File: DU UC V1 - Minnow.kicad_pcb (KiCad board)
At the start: 2 copper layers, 99 parts, among them J1201 USB_C_Receptacle_USB2.0_16P, J201 SODIMM-260, Q1001 BSS84, Q1201 MMBT3904, Q701 BSS84, Q901 AO3401A, Q902 AO3401A, U1001 MCP2558FD-xSN, U1201 PSM712-LF-T7, U301 3.3, U302 TPS7B8733QKVURQ1, U401 STM32F103CBTx, U501 STM32L552ZET6Q, U701 MCP2558FD-xSN, Y401 8MHz (7pF), Y501 32.768kHz, 1.2pF, Y502 16MHz, 7pF

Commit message: fixed like a bunch of things, power and new xcvr and lights and other goodies, also started layout
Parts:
- removed C1001, C1002, C1103, C1104, C310, C702: 100n, Capacitor_SMD:C_0603_1608Metric_Pad1.08x0.95mm_HandSolder
- removed C307, C308: 22u, Capacitor_SMD:C_0805_2012Metric_Pad1.18x1.45mm_HandSolder
- removed C309: 1u, Capacitor_SMD:C_0402_1005Metric_Pad0.74x0.62mm_HandSolder
- removed D1201: 600m, Diode_SMD:D_SOD-323_HandSoldering
- removed D902: 3V3, Diode_SMD:D_SMB
- removed D903, D904: BZT52C10-TP, Diode_SMD:D_SOD-123
- removed F901, F902: 500mA, Fuse:Fuse_1812_4532Metric
- removed J1201: USB_C_Receptacle_USB2.0_16P, Connector_USB:USB_C_Receptacle_Amphenol_124019772112A
- removed Q1001: BSS84, Package_TO_SOT_SMD:SOT-23
- removed Q1201: MMBT3904, Package_TO_SOT_SMD:SOT-23
- removed Q901, Q902: AO3401A, Package_TO_SOT_SMD:SOT-23-3
- removed R1001: 120, Resistor_SMD:R_0603_1608Metric_Pad0.98x0.95mm_HandSolder
- removed R1201: 10k, Resistor_SMD:R_0402_1005Metric_Pad0.72x0.64mm_HandSolder
- removed R1202: 36k, Resistor_SMD:R_0603_1608Metric_Pad0.98x0.95mm_HandSolder
- removed R1203: 1.5k, Resistor_SMD:R_0402_1005Metric_Pad0.72x0.64mm_HandSolder
- removed R1204, R1205: 5.1k, Resistor_SMD:R_0402_1005Metric_Pad0.72x0.64mm_HandSolder
- removed R1302, R1303, R1304, R1305: 22, Resistor_SMD:R_0402_1005Metric_Pad0.72x0.64mm_HandSolder
- removed U1001: MCP2558FD-xSN, Package_SO:SOIC-8_3.9x4.9mm_P1.27mm
- removed U1201: PSM712-LF-T7, Package_TO_SOT_SMD:SOT-23
- removed U302: TPS7B8733QKVURQ1, Package_TO_SOT_SMD:TO-252-5_TabPin3
- added C1501: 100n, Capacitor_SMD:C_0603_1608Metric_Pad1.08x0.95mm_HandSolder, F.Cu at (259.9, 107.5)
- added C1601: 100n, Capacitor_SMD:C_0402_1005Metric_Pad0.74x0.62mm_HandSolder, F.Cu at (280.4, 126.0)
- added C1602: 100n, Capacitor_SMD:C_0402_1005Metric_Pad0.74x0.62mm_HandSolder, F.Cu at (280.4, 127.9)
- added C1603: 100n, Capacitor_SMD:C_0402_1005Metric_Pad0.74x0.62mm_HandSolder, F.Cu at (280.4, 129.9)
- added C1604: 100n, Capacitor_SMD:C_0402_1005Metric_Pad0.74x0.62mm_HandSolder, F.Cu at (280.4, 131.9)
- added C1605: 100n, Capacitor_SMD:C_0402_1005Metric_Pad0.74x0.62mm_HandSolder, F.Cu at (280.4, 133.8)
- added C503: 100n, Capacitor_SMD:C_0402_1005Metric_Pad0.74x0.62mm_HandSolder, F.Cu at (175.9, 38.1)
- added C526: 4.7u, Capacitor_SMD:C_0603_1608Metric_Pad1.08x0.95mm_HandSolder, F.Cu at (105.7, 84.3)
- added C901: 100n, Capacitor_SMD:C_0402_1005Metric_Pad0.74x0.62mm_HandSolder, F.Cu at (136.4, 130.0)
- added C902: 100n, Capacitor_SMD:C_0402_1005Metric_Pad0.74x0.62mm_HandSolder, F.Cu at (138.6, 130.0)
- added C903: 100n, Capacitor_SMD:C_0402_1005Metric_Pad0.74x0.62mm_HandSolder, F.Cu at (137.5, 130.0)
- added D1101: Red, Diode_SMD:D_0603_1608Metric_Pad1.05x0.95mm_HandSolder, F.Cu at (157.8, 165.9)
- added D1102: Red, Diode_SMD:D_0603_1608Metric_Pad1.05x0.95mm_HandSolder, F.Cu at (154.1, 165.9)
- added D1103: Red, Diode_SMD:D_0603_1608Metric_Pad1.05x0.95mm_HandSolder, F.Cu at (156.0, 165.9)
- added D1104: Red, Diode_SMD:D_0603_1608Metric_Pad1.05x0.95mm_HandSolder, F.Cu at (159.7, 165.9)
- added D1105: Red, Diode_SMD:D_0603_1608Metric_Pad1.05x0.95mm_HandSolder, F.Cu at (152.2, 165.9)
- added D1106: Red, Diode_SMD:D_0603_1608Metric_Pad1.05x0.95mm_HandSolder, F.Cu at (146.6, 165.9)
- added D1107: Red, Diode_SMD:D_0603_1608Metric_Pad1.05x0.95mm_HandSolder, F.Cu at (150.4, 165.9)
- added D1108: Red, Diode_SMD:D_0603_1608Metric_Pad1.05x0.95mm_HandSolder, F.Cu at (148.5, 165.9)
- added D1301: Green, Diode_SMD:D_0805_2012Metric_Pad1.15x1.40mm_HandSolder, F.Cu at (249.1, 54.8)
- added D1401: 20V, Diode_SMD:D_SMB, F.Cu at (342.9, 82.8)
- added D1402: 20V, Diode_SMD:D_SMB, F.Cu at (316.1, 122.0)
- added D1501: White, Diode_SMD:D_0603_1608Metric_Pad1.05x0.95mm_HandSolder, F.Cu at (255.9, 98.8)
- added D1502: White, Diode_SMD:D_0603_1608Metric_Pad1.05x0.95mm_HandSolder, F.Cu at (255.9, 101.4)
- added D1701: 600m, Diode_SMD:D_SOD-323_HandSoldering, F.Cu at (327.5, 134.3)
- added D701: White, Diode_SMD:D_0603_1608Metric_Pad1.05x0.95mm_HandSolder, F.Cu at (232.6, 128.4)
- added D702: White, Diode_SMD:D_0603_1608Metric_Pad1.05x0.95mm_HandSolder, F.Cu at (243.4, 128.3)
- added J1701: MicroUSB, Connector_USB:USB_Micro-B_Amphenol_10118194-0001LF_Horizontal, F.Cu at (325.0, 151.4)
- added J1801: Conn_01x06_Pin, Connector_PinHeader_2.54mm:PinHeader_1x06_P2.54mm_Vertical, F.Cu at (313.6, 46.7)
- added J1802: Conn_01x04_Pin, Connector_PinHeader_2.54mm:PinHeader_1x04_P2.54mm_Vertical, F.Cu at (318.2, 46.7)
- added JP1001: NORFLASH_CLK, Jumper:SolderJumper-3_P1.3mm_Bridged2Bar12_Pad1.0x1.5mm_NumberLabels, F.Cu at (58.4, 92.5)
- added JP1002: NORFLASH_MISO, Jumper:SolderJumper-3_P1.3mm_Bridged2Bar12_Pad1.0x1.5mm_NumberLabels, F.Cu at (58.4, 96.0)
- added JP1003: NORFLASH_MOSI, Jumper:SolderJumper-3_P1.3mm_Bridged2Bar12_Pad1.0x1.5mm_NumberLabels, F.Cu at (58.4, 99.6)
- added JP1004: NORFLASH_NSS, Jumper:SolderJumper-3_P1.3mm_Bridged2Bar12_Pad1.0x1.5mm_NumberLabels, F.Cu at (58.4, 103.2)
- added JP1201: LEDARR_EN, Jumper:SolderJumper-3_P1.3mm_Bridged2Bar12_Pad1.0x1.5mm_NumberLabels, B.Cu at (125.8, 90.6)
- added JP1202: LEDARR_A0, Jumper:SolderJumper-3_P1.3mm_Bridged2Bar12_Pad1.0x1.5mm_NumberLabels, B.Cu at (125.8, 87.0)
- added JP1203: LEDARR_A1, Jumper:SolderJumper-3_P1.3mm_Bridged2Bar12_Pad1.0x1.5mm_NumberLabels, B.Cu at (125.8, 83.5)
- added JP1204: LEDARR_A2, Jumper:SolderJumper-3_P1.3mm_Bridged2Bar12_Pad1.0x1.5mm_NumberLabels, B.Cu at (125.8, 79.9)
- added JP1501: CAN_TERM, Jumper:SolderJumper-2_P1.3mm_Open_RoundedPad1.0x1.5mm, F.Cu at (251.0, 108.5)
- added JP1801: SolderJumper_2_Bridged, Jumper:SolderJumper-2_P1.3mm_Bridged_Pad1.0x1.5mm, F.Cu at (304.8, 46.2)
- added JP1802: SolderJumper_2_Bridged, Jumper:SolderJumper-2_P1.3mm_Bridged_Pad1.0x1.5mm, F.Cu at (304.8, 49.8)
- added JP1803: SolderJumper_2_Bridged, Jumper:SolderJumper-2_P1.3mm_Bridged_Pad1.0x1.5mm, F.Cu at (304.8, 53.3)
- added JP1804: SolderJumper_2_Bridged, Jumper:SolderJumper-2_P1.3mm_Bridged_Pad1.0x1.5mm, F.Cu at (304.8, 56.9)
- added JP1805: SolderJumper_2_Open, Jumper:SolderJumper-2_P1.3mm_Open_Pad1.0x1.5mm, F.Cu at (304.8, 60.4)
- added JP1806: SolderJumper_2_Open, Jumper:SolderJumper-2_P1.3mm_Open_Pad1.0x1.5mm, F.Cu at (309.1, 46.2)
- added JP1807: SolderJumper_2_Open, Jumper:SolderJumper-2_P1.3mm_Open_Pad1.0x1.5mm, F.Cu at (309.1, 49.8)
- added JP1808: SolderJumper_2_Open, Jumper:SolderJumper-2_P1.3mm_Open_Pad1.0x1.5mm, F.Cu at (309.1, 53.3)
- added JP301: AVDD_SEL, Jumper:SolderJumper-3_P1.3mm_Bridged2Bar12_Pad1.0x1.5mm_NumberLabels, F.Cu at (243.2, 44.5)
- added JP501: VDDUSB_SEL, Jumper:SolderJumper-3_P1.3mm_Bridged2Bar12_Pad1.0x1.5mm_NumberLabels, B.Cu at (72.5, 126.3)
- added JP502: VREF_SEL, Jumper:SolderJumper-3_P1.3mm_Bridged2Bar12_Pad1.0x1.5mm_NumberLabels, B.Cu at (72.5, 129.9)
- added JP503: VDDIO_SEL, Jumper:SolderJumper-3_P1.3mm_Bridged2Bar12_Pad1.0x1.5mm_NumberLabels, B.Cu at (72.5, 133.4)
- added JP504: JT_RST_SEL, Jumper:SolderJumper-3_P1.3mm_Bridged2Bar12_Pad1.0x1.5mm_NumberLabels, B.Cu at (72.5, 137.0)
- added JP701: CAN_TERM, Jumper:SolderJumper-2_P1.3mm_Open_RoundedPad1.0x1.5mm, F.Cu at (237.2, 126.4)
- added L501: 4.7u, bfr_inductors:BWVS005050404R7M00, F.Cu at (106.8, 88.3)
- added NT101: NetTie_2, NetTie:NetTie-2_SMD_Pad2.0mm, F.Cu at (173.0, 86.0)
- added Q1301: BSS84, Package_TO_SOT_SMD:SOT-23, F.Cu at (251.6, 55.0)
- added Q1501: BSS84, Package_TO_SOT_SMD:SOT-23, F.Cu at (251.2, 99.9)
- added Q1502: BSS84, Package_TO_SOT_SMD:SOT-23, F.Cu at (251.2, 104.5)
- added Q1701: MMBT3904, Package_TO_SOT_SMD:SOT-23, F.Cu at (322.5, 135.2)
- added Q702: BSS84, Package_TO_SOT_SMD:SOT-23, F.Cu at (241.6, 132.5)
- added R1101: 220, Resistor_SMD:R_0402_1005Metric_Pad0.72x0.64mm_HandSolder, F.Cu at (157.8, 162.8)
- added R1102: 220, Resistor_SMD:R_0402_1005Metric_Pad0.72x0.64mm_HandSolder, F.Cu at (154.1, 162.8)
- added R1103: 220, Resistor_SMD:R_0402_1005Metric_Pad0.72x0.64mm_HandSolder, F.Cu at (156.0, 162.8)
- added R1104: 220, Resistor_SMD:R_0402_1005Metric_Pad0.72x0.64mm_HandSolder, F.Cu at (159.7, 162.8)
- added R1105: 220, Resistor_SMD:R_0402_1005Metric_Pad0.72x0.64mm_HandSolder, F.Cu at (152.2, 162.8)
- added R1106: 220, Resistor_SMD:R_0402_1005Metric_Pad0.72x0.64mm_HandSolder, F.Cu at (146.6, 162.8)
- added R1107: 220, Resistor_SMD:R_0402_1005Metric_Pad0.72x0.64mm_HandSolder, F.Cu at (150.4, 162.8)
- added R1108: 220, Resistor_SMD:R_0402_1005Metric_Pad0.72x0.64mm_HandSolder, F.Cu at (148.5, 162.8)
- added R1401: 470, Resistor_SMD:R_0402_1005Metric_Pad0.72x0.64mm_HandSolder, F.Cu at (312.4, 119.1)
- added R1402: 360, Resistor_SMD:R_0603_1608Metric_Pad0.98x0.95mm_HandSolder, F.Cu at (312.4, 117.5)
- added R1403: 390, Resistor_SMD:R_0603_1608Metric_Pad0.98x0.95mm_HandSolder, F.Cu at (318.4, 116.7)
- added R1404: 270, Resistor_SMD:R_0603_1608Metric_Pad0.98x0.95mm_HandSolder, F.Cu at (347.4, 81.1)
- added R1405: 360, Resistor_SMD:R_0603_1608Metric_Pad0.98x0.95mm_HandSolder, F.Cu at (347.4, 83.6)
- added R1406: 390, Resistor_SMD:R_0603_1608Metric_Pad0.98x0.95mm_HandSolder, F.Cu at (347.4, 86.2)
- added R1407: 100k, Resistor_SMD:R_0402_1005Metric_Pad0.72x0.64mm_HandSolder, F.Cu at (316.1, 116.4)
- added R1408: 100k, Resistor_SMD:R_0402_1005Metric_Pad0.72x0.64mm_HandSolder, F.Cu at (351.2, 82.9)
- added R1501: 120, Resistor_SMD:R_0402_1005Metric_Pad0.72x0.64mm_HandSolder, F.Cu at (260.5, 103.7)
- added R1502: 120, Resistor_SMD:R_0603_1608Metric_Pad0.98x0.95mm_HandSolder, F.Cu at (260.3, 98.8)
- added R1503: 120, Resistor_SMD:R_0603_1608Metric_Pad0.98x0.95mm_HandSolder, F.Cu at (260.3, 101.3)
- added R1701: 10k, Resistor_SMD:R_0402_1005Metric_Pad0.72x0.64mm_HandSolder, F.Cu at (317.4, 147.3)
- added R1702: 36k, Resistor_SMD:R_0603_1608Metric_Pad0.98x0.95mm_HandSolder, F.Cu at (318.5, 144.8)
- added R1703: 1.5k, Resistor_SMD:R_0402_1005Metric_Pad0.72x0.64mm_HandSolder, F.Cu at (317.4, 139.7)
- added R1704: 100k, Resistor_SMD:R_0402_1005Metric_Pad0.72x0.64mm_HandSolder, F.Cu at (317.4, 137.1)
- added R1801: 10k, Resistor_SMD:R_0402_1005Metric_Pad0.72x0.64mm_HandSolder, F.Cu at (322.1, 45.4)
- added R1802: 22, Resistor_SMD:R_0402_1005Metric_Pad0.72x0.64mm_HandSolder, F.Cu at (322.1, 47.4)
- added R1803: 22, Resistor_SMD:R_0402_1005Metric_Pad0.72x0.64mm_HandSolder, F.Cu at (322.1, 49.4)
- added R1804: 22, Resistor_SMD:R_0402_1005Metric_Pad0.72x0.64mm_HandSolder, F.Cu at (322.1, 51.4)
- added R1805: 22, Resistor_SMD:R_0402_1005Metric_Pad0.72x0.64mm_HandSolder, F.Cu at (322.1, 53.4)
- added R702: 120, Resistor_SMD:R_0603_1608Metric_Pad0.98x0.95mm_HandSolder, F.Cu at (234.5, 128.4)
- added R703: 120, Resistor_SMD:R_0603_1608Metric_Pad0.98x0.95mm_HandSolder, F.Cu at (241.6, 128.3)
- added R903: 47k, Resistor_SMD:R_0402_1005Metric_Pad0.72x0.64mm_HandSolder, F.Cu at (137.5, 138.0)
- added R904: 47k, Resistor_SMD:R_0402_1005Metric_Pad0.72x0.64mm_HandSolder, F.Cu at (129.0, 133.1)
- added R905: 47k, Resistor_SMD:R_0402_1005Metric_Pad0.72x0.64mm_HandSolder, F.Cu at (129.0, 135.6)
- added R906: 47k, Resistor_SMD:R_0402_1005Metric_Pad0.72x0.64mm_HandSolder, F.Cu at (139.9, 133.1)
- added SW401: STLINK_RST, Button_Switch_SMD:SW_Push_1P1T-SH_NO_CK_KMR2xxG, F.Cu at (260.9, 147.7)
- added SW501: MCU_RST, Button_Switch_SMD:SW_Push_1P1T-SH_NO_CK_KMR2xxG, F.Cu at (72.0, 142.3)
- added U1101: 74HC4051, Package_SO:TSSOP-16_4.4x5mm_P0.65mm, F.Cu at (153.2, 157.6)
- added U1401: TPS25961, Package_SON:WSON-6-1EP_2x2mm_P0.65mm_EP1x1.6mm, F.Cu at (316.1, 118.4)
- added U1402: TPS25961, Package_SON:WSON-6-1EP_2x2mm_P0.65mm_EP1x1.6mm, F.Cu at (351.7, 85.7)
- added U1501: TCAN334G, Package_TO_SOT_SMD:TSOT-23-8, F.Cu at (256.3, 105.1)
- added U1701: PSM712-LF-T7, Package_TO_SOT_SMD:SOT-23, F.Cu at (322.5, 139.9)
- added U901: MX25R3235FM2xx1, Package_SO:SOIC-8_5.3x5.3mm_P1.27mm, F.Cu at (134.5, 134.3)
- C1101, C1102, C520: footprint Capacitor_SMD:C_0603_1608Metric_Pad1.08x0.95mm_HandSolder -> Capacitor_SMD:C_0402_1005Metric_Pad0.74x0.62mm_HandSolder
- C203, C204, R401, R402, R407, R408: moved to B.Cu
- C301, C303: value 22u -> 1u; footprint Capacitor_SMD:C_0805_2012Metric_Pad1.18x1.45mm_HandSolder -> Capacitor_SMD:C_0402_1005Metric_Pad0.74x0.62mm_HandSolder
- C304, C305, C306: value 100n -> 1u; footprint Capacitor_SMD:C_0603_1608Metric_Pad1.08x0.95mm_HandSolder -> Capacitor_SMD:C_0402_1005Metric_Pad0.74x0.62mm_HandSolder
- C509: value 100n -> 22p
- C511: value 22p -> 100n
- C512, C514, C515, C516, C519, C522: value 1u -> 100n
- C517: value 1u -> 100n; footprint Capacitor_SMD:C_0402_1005Metric_Pad0.74x0.62mm_HandSolder -> Capacitor_SMD:C_0603_1608Metric_Pad1.08x0.95mm_HandSolder
- C518, C521, C523, C524: value 10u -> 100n; footprint Capacitor_SMD:C_0603_1608Metric_Pad1.08x0.95mm_HandSolder -> Capacitor_SMD:C_0402_1005Metric_Pad0.74x0.62mm_HandSolder
- C525: value 4.7u -> 100n; footprint Capacitor_SMD:C_0603_1608Metric_Pad1.08x0.95mm_HandSolder -> Capacitor_SMD:C_0402_1005Metric_Pad0.74x0.62mm_HandSolder
- D901: value 4V7 -> 3V3; footprint Diode_SMD:D_SMB -> Diode_SMD:D_SOD-123
- J201: footprint Connector_PCBEdge:SODIMM-260_DDR4_H4.0-5.2_OrientationStd_Socket -> bfr_connectors:SODIMM-260 DDR4
- R1301: value 10k -> 120; footprint Resistor_SMD:R_0402_1005Metric_Pad0.72x0.64mm_HandSolder -> Resistor_SMD:R_0603_1608Metric_Pad0.98x0.95mm_HandSolder
- R701: footprint Resistor_SMD:R_0603_1608Metric_Pad0.98x0.95mm_HandSolder -> Resistor_SMD:R_0402_1005Metric_Pad0.72x0.64mm_HandSolder
- R901, R902: value 100k -> 47k; footprint Resistor_SMD:R_0603_1608Metric_Pad0.98x0.95mm_HandSolder -> Resistor_SMD:R_0402_1005Metric_Pad0.72x0.64mm_HandSolder
- U301: value 3.3 -> TPS7B8733QKVURQ1; footprint Package_TO_SOT_SMD:SOT-223-3_TabPin2 -> Package_TO_SOT_SMD:TO-252-5_TabPin3
- U701: value MCP2558FD-xSN -> TCAN334G; footprint Package_SO:SOIC-8_3.9x4.9mm_P1.27mm -> Package_TO_SOT_SMD:TSOT-23-8
- Y401: value 8MHz (7pF) -> 8MHz 5pF; footprint Crystal:Crystal_HC49-4H_Vertical -> Crystal:Crystal_SMD_5032-2Pin_5.0x3.2mm_HandSoldering
- moved C517 153.6 mm to (66.5, 134.5)
- moved U401 132.0 mm to (269.1, 139.8)
- moved C514 131.3 mm to (85.8, 52.5)
- moved C519 130.7 mm to (89.1, 50.5)
- moved C522 129.5 mm to (89.1, 56.4)
- moved R501 124.1 mm to (94.7, 118.8)
- moved C504 117.7 mm to (98.0, 46.3)
- moved C506 117.7 mm to (98.0, 50.2)
- moved C512 116.2 mm to (101.3, 50.2)
- moved C203 114.0 mm to (82.0, 72.4), turned to -90 degrees
- moved C202 113.9 mm to (82.0, 72.4), turned to 90 degrees
- moved Y501 113.3 mm to (107.9, 124.6)
- moved C204 112.6 mm to (83.6, 72.4), turned to -90 degrees
- moved C201 112.3 mm to (83.6, 72.4), turned to 90 degrees
- moved C1101 106.2 mm to (155.5, 153.0)
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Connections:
- net /Power/3V3_RAW renamed /5V_RAW
- net /Power/5V_RAW renamed /3V3A_RAW
- C1101 pad 1: +3.3V -> GND
- C1101 pad 2: GND -> +3.3V
- C1102 pad 1: +3.3V -> GND
- C1102 pad 2: GND -> +3.3V
- C201 pad 1: GNDPWR -> GND
- C202 pad 1: GNDPWR -> GND
- C301 pad 1: +5V -> /Power/Power Protection/5V_PROT
- C302 pad 1: +5V -> /Power/Power Protection/5V_PROT
- C303 pad 1: Net-(JP301-B) -> /Power/Power Protection/5V_PROT
- C304 pad 1: +5V -> +3.3V
- C305 pad 1: Net-(JP301-B) -> +3.3V
- C504 pad 1: +3.3VA -> +3.3V
- C505 pad 1: +3.3V -> +3.3VA
- C506 pad 1: +3.3VA -> +3.3V
- C507 pad 1: +3.3V -> +3.3VA
- C508 pad 1: +3.3VA -> +3.3V
- C509 pad 1: +3.3V -> Net-(U501I-PH0/HSE_OSC_IN)
- C510 pad 1: Net-(U501I-PH0/HSE_OSC_IN) -> Net-(U501I-PH1/HSE_OSC_OUT)
- C511 pad 1: Net-(U501I-PH1/HSE_OSC_OUT) -> +3.3VA
- C512 pad 1: +3.3VA -> +3.3V
- C513 pad 1: +3.3V -> +3.3VA
- C514 pad 1: +3.3VA -> +3.3V
- C515 pad 1: +3.3V -> +3.3VA
- C516 pad 1: +3.3VA -> +3.3V
- C517 pad 1: +3.3V -> Net-(JP504-A)
- C520 pad 1: Net-(JP504-A) -> +3.3VA
- C521 pad 1: +3.3VA -> +3.3V
- C525 pad 1: Net-(C525-Pad1) -> +3.3V
- C701 pad 1: /STM32L552ZET6Q/Peripherals/+5V -> +3.3V
- D901 pad 1: Net-(D901-K) -> +3.3V
- D901 pad 2: GNDPWR -> GND
- J201 pad 102: /SODIMM Connector/PB15 -> /SODIMM Connector/PB2
- J201 pad 103: /SODIMM Connector/PB0 -> /SODIMM Connector/PC9
- J201 pad 106: /SODIMM Connector/PD1 -> /SODIMM Connector/PB1
- J201 pad 107: /SODIMM Connector/PC0 -> /SODIMM Connector/PC10
- J201 pad 11: GNDPWR -> GND
- J201 pad 110: /SODIMM Connector/PD2 -> /SODIMM Connector/PB0
- J201 pad 111: /SODIMM Connector/PC1 -> /SODIMM Connector/PC11
- J201 pad 114: /SODIMM Connector/PD3 -> /SODIMM Connector/PA7
- J201 pad 115: /SODIMM Connector/PC2 -> /SODIMM Connector/PC12
- J201 pad 118: /SODIMM Connector/PD4 -> /SODIMM Connector/PA6
- J201 pad 119: /SODIMM Connector/PC3 -> /SODIMM Connector/PA8
- J201 pad 122: /SODIMM Connector/PD5 -> /SODIMM Connector/PA5
- J201 pad 123: /SODIMM Connector/PC6 -> /SODIMM Connector/PA9
- J201 pad 126: /SODIMM Connector/PD6 -> /SODIMM Connector/PA4
- J201 pad 127: /SODIMM Connector/PC7 -> /SODIMM Connector/PA10
- J201 pad 13: GNDPWR -> GND
- J201 pad 130: /SODIMM Connector/PD7 -> /SODIMM Connector/PA3
- J201 pad 131: /SODIMM Connector/PC8 -> /SODIMM Connector/PA15
- J201 pad 134: /SODIMM Connector/PD8 -> /SODIMM Connector/PA2
- J201 pad 135: /SODIMM Connector/PC9 -> /SODIMM Connector/PD0
- J201 pad 138: /SODIMM Connector/PD9 -> /SODIMM Connector/PA1
- J201 pad 139: /SODIMM Connector/PC10 -> /SODIMM Connector/PD1
- J201 pad 142: /SODIMM Connector/PD10 -> /SODIMM Connector/PA0
- J201 pad 143: /SODIMM Connector/PC11 -> /SODIMM Connector/PD2
- J201 pad 146: /SODIMM Connector/PD11 -> /SODIMM Connector/PC3
- J201 pad 147: /SODIMM Connector/PC12 -> /SODIMM Connector/PD3
- J201 pad 15: GNDPWR -> GND
- J201 pad 150: /SODIMM Connector/PD12 -> /SODIMM Connector/PC2
- J201 pad 151: /SODIMM Connector/PC13 -> /SODIMM Connector/PD4
- J201 pad 154: /SODIMM Connector/PD13 -> /SODIMM Connector/PC1
- J201 pad 155: /SODIMM Connector/PD0 -> /SODIMM Connector/PD5
- J201 pad 158: /SODIMM Connector/PF11 -> /SODIMM Connector/PC0
- J201 pad 159: /SODIMM Connector/PD14 -> /SODIMM Connector/PD6
- J201 pad 162: /SODIMM Connector/PF12 -> /SODIMM Connector/PF10
- J201 pad 163: /SODIMM Connector/PD15 -> /SODIMM Connector/PD7
- J201 pad 166: /SODIMM Connector/PF13 -> /SODIMM Connector/PF9
- J201 pad 167: /SODIMM Connector/PF0 -> /SODIMM Connector/PG9
- J201 pad 17: GNDPWR -> GND
- J201 pad 170: /SODIMM Connector/PF14 -> /SODIMM Connector/PF8
- J201 pad 171: /SODIMM Connector/PF1 -> /SODIMM Connector/PG10
- J201 pad 174: /SODIMM Connector/PF15 -> /SODIMM Connector/PF7
- J201 pad 175: /SODIMM Connector/PF2 -> /SODIMM Connector/PG12
- J201 pad 178: /SODIMM Connector/PE0 -> /SODIMM Connector/PF6
- J201 pad 179: /SODIMM Connector/PF3 -> /SODIMM Connector/PG13
- J201 pad 182: /SODIMM Connector/PE1 -> /SODIMM Connector/PF5
- J201 pad 183: /SODIMM Connector/PF4 -> /SODIMM Connector/PG14
- J201 pad 186: /SODIMM Connector/PE2 -> /SODIMM Connector/PF4
- J201 pad 187: /SODIMM Connector/PF5 -> /SODIMM Connector/PG15
- J201 pad 19: GNDPWR -> GND
- J201 pad 190: /SODIMM Connector/PE3 -> /SODIMM Connector/PF3
- J201 pad 191: /SODIMM Connector/PF6 -> /SODIMM Connector/PB4
- J201 pad 194: /SODIMM Connector/PE4 -> /SODIMM Connector/PF2
- J201 pad 195: /SODIMM Connector/PF7 -> /SODIMM Connector/PB5
- J201 pad 198: /SODIMM Connector/PE5 -> /SODIMM Connector/PF1
- J201 pad 199: /SODIMM Connector/PF8 -> /SODIMM Connector/PB6
- J201 pad 202: /SODIMM Connector/PE6 -> /SODIMM Connector/PF0
- J201 pad 203: /SODIMM Connector/PF9 -> /SODIMM Connector/PB7
- J201 pad 206: /SODIMM Connector/PE7 -> /SODIMM Connector/PC13
- J201 pad 207: /SODIMM Connector/PF10 -> /SODIMM Connector/PB8
- J201 pad 209: /SODIMM Connector/PE8 -> GND
- J201 pad 211: GND -> /SODIMM Connector/PB9
- J201 pad 212: GND -> /NOR Flash/WRITE_PROT
- J201 pad 213: /SODIMM Connector/PE9 -> GND
- J201 pad 215: GND -> /SODIMM Connector/PE0
- J201 pad 216: GND -> /NOR Flash/HOLD
- J201 pad 217: /SODIMM Connector/PE10 -> GND
- J201 pad 219: GND -> /SODIMM Connector/PE1
- J201 pad 22: /SODIMM Connector/CANL_STLINK -> /CANL_STLINK
- J201 pad 220: GND -> /SODIMM Connector/VBATT
- J201 pad 221: /SODIMM Connector/PE11 -> GND
- J201 pad 222: GND -> /SODIMM Connector/VBATT
- J201 pad 223: GND -> /SODIMM Connector/PE2
- J201 pad 225: /SODIMM Connector/PE12 -> GND
- J201 pad 227: GND -> /SODIMM Connector/PE3
- J201 pad 228: /SODIMM Connector/VBATT -> /SODIMM Connector/VDDIO
- J201 pad 229: /SODIMM Connector/PE13 -> GND
- J201 pad 230: /SODIMM Connector/VBATT -> /SODIMM Connector/VDDIO
- J201 pad 231: GND -> /SODIMM Connector/PE4
- J201 pad 232: /SODIMM Connector/VBATT -> /SODIMM Connector/VDDIO
- J201 pad 233: /SODIMM Connector/PE14 -> GND
- J201 pad 234: /SODIMM Connector/VBATT -> /SODIMM Connector/VDDIO
- J201 pad 235: GND -> /SODIMM Connector/PE5
- J201 pad 237: /SODIMM Connector/PE15 -> GND
- J201 pad 239: GND -> /SODIMM Connector/PE6
- J201 pad 24: /SODIMM Connector/CANH_STLINK -> /CANH_STLINK
- J201 pad 244: /SODIMM Connector/VDDIO -> /SODIMM Connector/VREF
- J201 pad 246: /SODIMM Connector/VDDIO -> /SODIMM Connector/VREF
- J201 pad 248: /SODIMM Connector/VDDIO -> /SODIMM Connector/VREF
- J201 pad 249: /SODIMM Connector/VDDUSB -> GND
- J201 pad 250: /SODIMM Connector/VDDIO -> GND
- J201 pad 255: GND -> unconnected-(J201-Pad255)
- J201 pad 256: /SODIMM Connector/VREF -> GND
- J201 pad 257: GND -> unconnected-(J201-Pad257)
- J201 pad 258: /SODIMM Connector/VREF -> GND
- J201 pad 259: GND -> unconnected-(J201-Pad259)
- J201 pad 260: /SODIMM Connector/VREF -> GND
- J201 pad 27: /SODIMM Connector/PG0 -> /SODIMM Connector/PB13
- J201 pad 30: /SODIMM Connector/PG9 -> /SODIMM Connector/PB11
- J201 pad 31: /SODIMM Connector/PG1 -> /SODIMM Connector/PB14
- J201 pad 34: /SODIMM Connector/PG10 -> /SODIMM Connector/PB10
- J201 pad 35: /SODIMM Connector/PG2 -> /SODIMM Connector/PB15
- J201 pad 38: /SODIMM Connector/PG12 -> /SODIMM Connector/PE15
- J201 pad 39: /SODIMM Connector/PG3 -> /SODIMM Connector/PD8
- J201 pad 42: /SODIMM Connector/PG13 -> /SODIMM Connector/PE14
- J201 pad 43: /SODIMM Connector/PG4 -> /SODIMM Connector/PD9
- J201 pad 46: /SODIMM Connector/PG14 -> /SODIMM Connector/PE13
- J201 pad 47: /SODIMM Connector/PG5 -> /SODIMM Connector/PD10
- J201 pad 50: /SODIMM Connector/PG15 -> /SODIMM Connector/PE12
- J201 pad 51: /SODIMM Connector/PG6 -> /SODIMM Connector/PD11
- J201 pad 54: /SODIMM Connector/PB1 -> /SODIMM Connector/PE11
- J201 pad 55: /SODIMM Connector/PA0 -> /SODIMM Connector/PD12
- J201 pad 58: /SODIMM Connector/PB2 -> /SODIMM Connector/PE10
- J201 pad 59: /SODIMM Connector/PA1 -> /SODIMM Connector/PD13
- J201 pad 62: /SODIMM Connector/PB4 -> /SODIMM Connector/PE9
- J201 pad 63: /SODIMM Connector/PA2 -> /SODIMM Connector/PD14
- J201 pad 66: /SODIMM Connector/PB5 -> /SODIMM Connector/PE8
- J201 pad 67: /SODIMM Connector/PA3 -> /SODIMM Connector/PD15
- J201 pad 70: /SODIMM Connector/PB6 -> /SODIMM Connector/PE7
- J201 pad 71: /SODIMM Connector/PA4 -> /SODIMM Connector/PG2
- J201 pad 74: /SODIMM Connector/PB7 -> /SODIMM Connector/PG1
- J201 pad 75: /SODIMM Connector/PA5 -> /SODIMM Connector/PG3
- J201 pad 78: /SODIMM Connector/PB8 -> /SODIMM Connector/PG0
- J201 pad 79: /SODIMM Connector/PA6 -> /SODIMM Connector/PG4
- J201 pad 82: /SODIMM Connector/PB9 -> /SODIMM Connector/PF15
- J201 pad 83: /SODIMM Connector/PA7 -> /SODIMM Connector/PG5
- J201 pad 86: /SODIMM Connector/PB10 -> /SODIMM Connector/PF14
- J201 pad 87: /SODIMM Connector/PA8 -> /SODIMM Connector/PG6
- J201 pad 90: /SODIMM Connector/PB11 -> /SODIMM Connector/PF13
- J201 pad 91: /SODIMM Connector/PA9 -> /SODIMM Connector/PC6
- J201 pad 94: /SODIMM Connector/PB13 -> /SODIMM Connector/PF12
- J201 pad 95: /SODIMM Connector/PA10 -> /SODIMM Connector/PC7
- J201 pad 98: /SODIMM Connector/PB14 -> /SODIMM Connector/PF11
- J201 pad 99: /SODIMM Connector/PA15 -> /SODIMM Connector/PC8
- Q701 pad 1: /STM32L552ZET6Q/Peripherals/CAN2_TX -> /STM32L552ZET6Q/CAN2_TX
- Q701 pad 2: Net-(Q701-S) -> +3.3V
- Q701 pad 3: +3.3V -> Net-(Q701-D)
- R1301 pad 1: GND -> Net-(D1301-A)
- R701 pad 1: GND -> /SODIMM Connector/CANL_MCU
- R701 pad 2: Net-(Q701-S) -> Net-(JP701-B)
- R901 pad 1: GNDPWR -> /NOR Flash/CS
- R901 pad 2: Net-(D903-A) -> +3.3V
- R902 pad 1: GNDPWR -> /NOR Flash/CLK
- R902 pad 2: Net-(D904-A) -> +3.3V
- U301 pad 1: GNDPWR -> /Power/Power Protection/5V_PROT
- U301 pad 2: +3.3V -> /Power/Diagnostic LED/Vin
- U301 pad 3: Net-(JP301-B) -> GNDPWR
- U401 pad 14: unconnected-(U401-PA4-Pad14) -> /ST-link V2/CS
- U401 pad 39: unconnected-(U401-PB3-Pad39) -> /ST-link V2/CLK
- U401 pad 40: unconnected-(U401-PB4-Pad40) -> /ST-link V2/MISO
- U401 pad 41: unconnected-(U401-PB5-Pad41) -> /ST-link V2/MOSI
- U501 pad 110: /SODIMM Connector/PA15 -> /STM32L552ZET6Q/Peripherals/PA15_IN
- U501 pad 111: /SODIMM Connector/PC10 -> /STM32L552ZET6Q/Peripherals/PC10_IN
- U501 pad 112: /SODIMM Connector/PC11 -> /STM32L552ZET6Q/Peripherals/PC11_IN
- U501 pad 113: /SODIMM Connector/PC12 -> /STM32L552ZET6Q/Peripherals/PC12_IN
- U501 pad 143: Net-(C525-Pad1) -> Net-(C526-Pad1)
- U501 pad 47: /SODIMM Connector/PF12 -> /STM32L552ZET6Q/Peripherals/PF_IN12
- U501 pad 50: /SODIMM Connector/PF13 -> /STM32L552ZET6Q/Peripherals/PF_IN13
- U501 pad 51: /SODIMM Connector/PF14 -> /STM32L552ZET6Q/Peripherals/PF_IN14
- U501 pad 52: /SODIMM Connector/PF15 -> /STM32L552ZET6Q/Peripherals/PF_IN15
- U501 pad 72: Net-(C525-Pad1) -> Net-(C526-Pad1)
- U701 pad 1: /STM32L552ZET6Q/Peripherals/CAN2_TX -> /STM32L552ZET6Q/CAN2_TX
- U701 pad 3: /STM32L552ZET6Q/Peripherals/+5V -> +3.3V
- U701 pad 4: /STM32L552ZET6Q/Peripherals/CAN2_RX -> /STM32L552ZET6Q/CAN2_RX
- U701 pad 5: +3.3V -> GND
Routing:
- added copper zone on B.Cu, net GND
- added copper zone on F.Cu, net GND
- added copper zone on In1.Cu, net GND
- added copper zone on In2.Cu, net GND
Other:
- board outline added: 30 x 69.6 mm
- copper layers 2 -> 4

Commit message: quicksave on some R.S. T.S. (mostly layout changes, small pin changes for better routing)
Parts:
- removed C524, C525: 100n, Capacitor_SMD:C_0402_1005Metric_Pad0.74x0.62mm_HandSolder
- C1101, C1102, C1501, C1601, C1602, C1603, C1604, C1605, C201, C202, C301, C302, C303, C304, C305, C306, C403, C504, C506, C508, C512, C514, C516, C517, C519, C521, C522, C523, D1401, JP1001, JP1002, JP1003, JP1004, JP1501, Q1301, R1301, R1404, R1405, R1406, R1408, R1501, R1502, R1503, R1701, R1702, R1704, R403, R404, R405, R501, U1402: moved to B.Cu
- C203, C204: moved to F.Cu
- J1701: footprint Connector_USB:USB_Micro-B_Amphenol_10118194-0001LF_Horizontal -> Connector_USB:USB_Micro-B_Molex-105133-0001
- moved U1402 260.3 mm to (91.7, 74.3), turned to -90 degrees
- moved R1408 257.7 mm to (93.6, 74.3), turned to 90 degrees
- moved D1401 255.8 mm to (87.2, 74.4)
- moved R1404 255.7 mm to (91.7, 76.7), turned to 180 degrees
- moved R1406 254.8 mm to (93.0, 71.6), turned to 180 degrees
- moved R1405 252.4 mm to (95.2, 74.3), turned to -90 degrees
- moved D1402 233.8 mm to (87.2, 74.4), turned to -90 degrees
- moved R1403 229.6 mm to (92.2, 77.2), turned to 180 degrees
- moved U1401 229.5 mm to (90.9, 74.4), turned to 90 degrees
- moved J1701 227.2 mm to (111.8, 73.0)
- moved R1407 227.2 mm to (92.8, 74.4), turned to -90 degrees
- moved R1401 226.5 mm to (90.8, 72.1), turned to 180 degrees
- moved R1402 222.4 mm to (94.2, 74.4), turned to 90 degrees
- moved U1701 220.9 mm to (110.3, 78.3), turned to 90 degrees
- moved D1701 220.9 mm to (114.3, 76.4), turned to 180 degrees
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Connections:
- net /Power/Diagnostic LED/Vin renamed /Power/Diagnostic LED/SIG
- net Net-(D1701-A) renamed /ST-link V2/USB Micro-B/PP5000_VUSB_RAW
- net Net-(J1701-ID) renamed /ST-link V2/USB Micro-B/USB_ID
- C201 pad 1: GND -> /3V3A_RAW
- C201 pad 2: /3V3A_RAW -> GND
- C202 pad 1: GND -> /3V3A_RAW
- C202 pad 2: /3V3A_RAW -> GND
- D1401 pad 1: /Power/Power Protection/3V3_RAW -> /3V3A_RAW
- D1401 pad 2: GNDPWR -> GND
- J201 pad 1: /3V3A_RAW -> /5V_RAW
- J201 pad 10: /5V_RAW -> GND
- J201 pad 11: GND -> GNDPWR
- J201 pad 12: GNDPWR -> /3V3A_RAW
- J201 pad 13: GND -> GNDPWR
- J201 pad 14: GNDPWR -> /3V3A_RAW
- J201 pad 15: GND -> GNDPWR
- J201 pad 16: GNDPWR -> /3V3A_RAW
- J201 pad 17: GND -> GNDPWR
- J201 pad 18: GNDPWR -> /3V3A_RAW
- J201 pad 19: GND -> GNDPWR
- J201 pad 2: /5V_RAW -> GND
- J201 pad 20: GNDPWR -> /3V3A_RAW
- J201 pad 3: /3V3A_RAW -> /5V_RAW
- J201 pad 4: /5V_RAW -> GND
- J201 pad 5: /3V3A_RAW -> /5V_RAW
- J201 pad 6: /5V_RAW -> GND
- J201 pad 7: /3V3A_RAW -> /5V_RAW
- J201 pad 8: /5V_RAW -> GND
- J201 pad 9: /3V3A_RAW -> /5V_RAW
- JP1001 pad 1: /STM32L552ZET6Q/Peripherals/NORFLASH Select/PC_IN10 -> /STM32L552ZET6Q/Peripherals/PC_IN10
- JP1002 pad 1: /STM32L552ZET6Q/Peripherals/NORFLASH Select/PC_IN11 -> /STM32L552ZET6Q/Peripherals/PC_IN11
- JP1003 pad 1: /STM32L552ZET6Q/Peripherals/NORFLASH Select/PC_IN12 -> /STM32L552ZET6Q/Peripherals/PC_IN12
- JP301 pad 3: /Power/3V3A_PROT -> /Power/Power Protection/3V3A_PROT
- R1404 pad 2: /Power/Power Protection/3V3_RAW -> /3V3A_RAW
- R1406 pad 1: GNDPWR -> GND
- R1408 pad 1: GNDPWR -> GND
- U1402 pad 1: /Power/Power Protection/3V3_PROT -> /Power/Power Protection/3V3A_PROT
- U1402 pad 4: GNDPWR -> GND
- U1402 pad 6: /Power/Power Protection/3V3_RAW -> /3V3A_RAW
- U1402 pad 7: GNDPWR -> GND
- U501 pad 111: /STM32L552ZET6Q/Peripherals/PC10_IN -> /STM32L552ZET6Q/Peripherals/PC_IN10
- U501 pad 112: /STM32L552ZET6Q/Peripherals/PC11_IN -> /STM32L552ZET6Q/Peripherals/PC_IN11
- U501 pad 113: /STM32L552ZET6Q/Peripherals/PC12_IN -> /STM32L552ZET6Q/Peripherals/PC_IN12

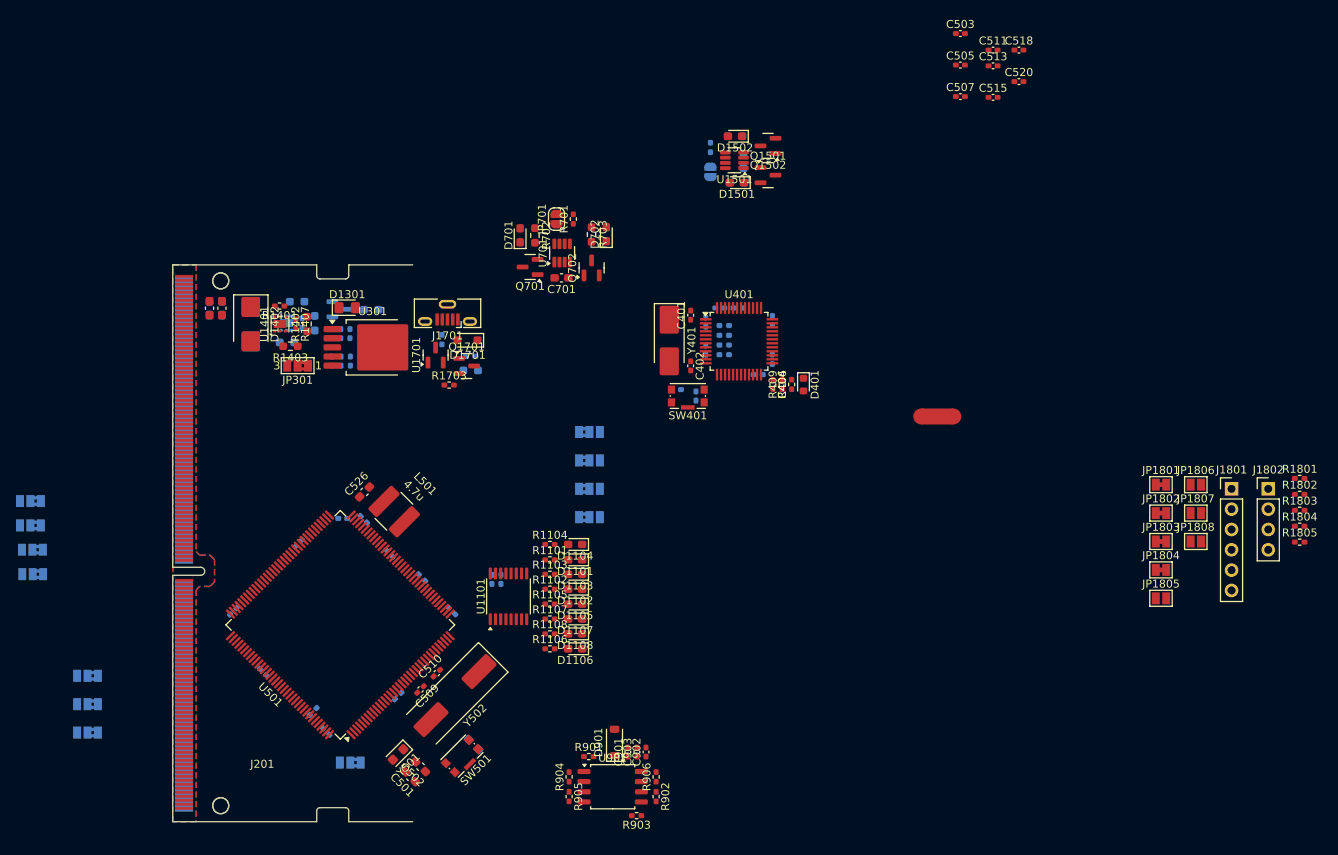
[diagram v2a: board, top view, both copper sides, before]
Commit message: laid out most of power, main xcvr, prob some other stuff
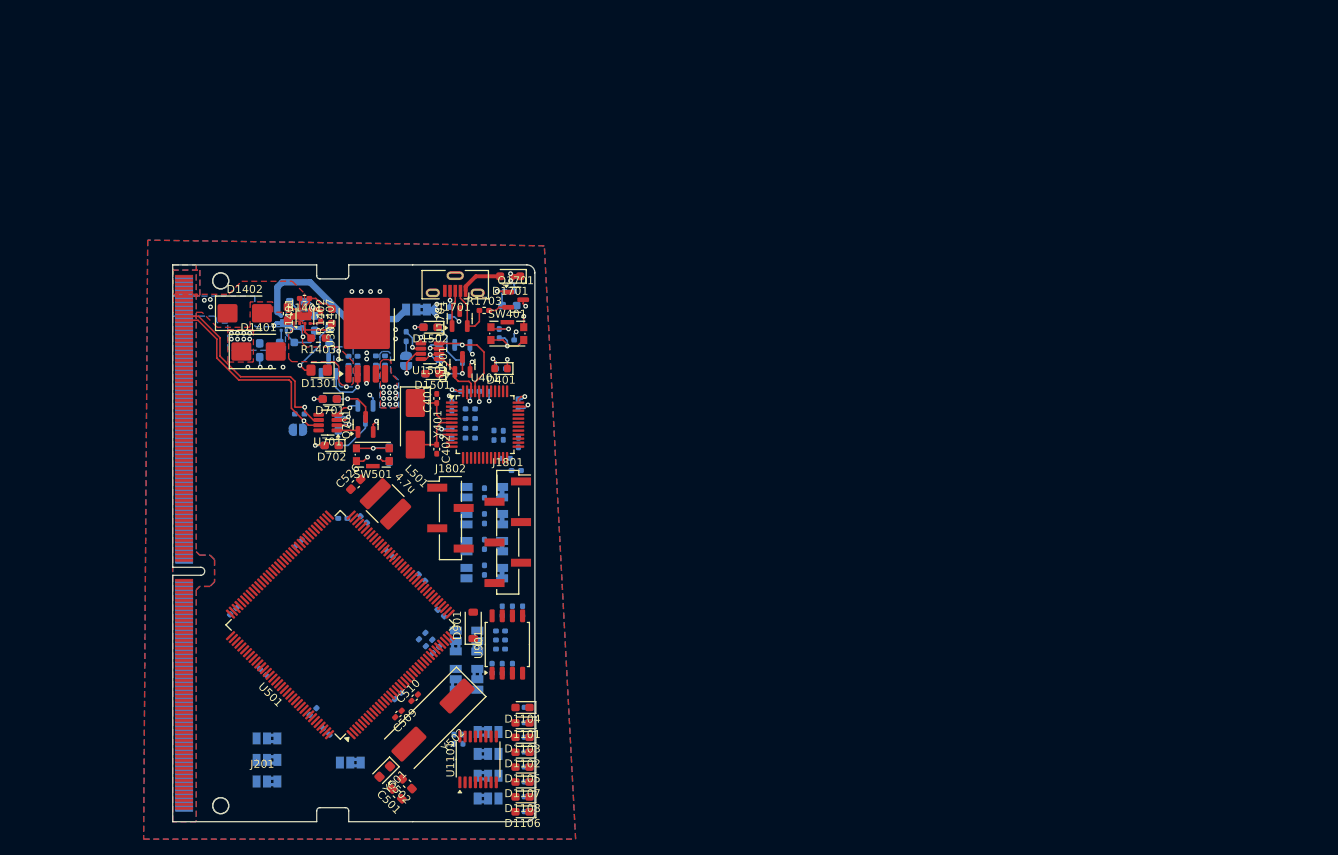
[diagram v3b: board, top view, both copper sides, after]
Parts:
- removed C202, C204: 10u, Capacitor_SMD:C_0603_1608Metric_Pad1.08x0.95mm_HandSolder
- removed C511, C513, C515, C518, C520: 100n, Capacitor_SMD:C_0402_1005Metric_Pad0.74x0.62mm_HandSolder
- removed NT101: NetTie_2, NetTie:NetTie-2_SMD_Pad2.0mm
- C404, C503, C505, C507, C701, C901, C902, C903, JP1801, JP1802, JP1803, JP1804, JP1805, JP1806, JP1807, JP1808, JP301, JP701, Q1502, Q702, R1101, R1102, R1103, R1104, R1105, R1106, R1107, R1108, R1801, R1802, R1803, R1804, R1805, R406, R409, R701, R702, R703, R901, R902, R903, R904, R905, R906: moved to B.Cu
- D1401: moved to F.Cu
- J1801: footprint Connector_PinHeader_2.54mm:PinHeader_1x06_P2.54mm_Vertical -> Connector_PinHeader_2.54mm:PinHeader_1x06_P2.54mm_Vertical_SMD_Pin1Right
- J1802: footprint Connector_PinHeader_2.54mm:PinHeader_1x04_P2.54mm_Vertical -> Connector_PinHeader_2.54mm:PinHeader_1x04_P2.54mm_Vertical_SMD_Pin1Left
- moved J1802 102.3 mm to (112.2, 98.7)
- moved R1805 102.0 mm to (116.4, 105.2), turned to 90 degrees
- moved R1804 101.9 mm to (116.4, 101.9), turned to 90 degrees
- moved R1803 101.9 mm to (116.4, 98.7), turned to 90 degrees
- moved R1802 101.9 mm to (116.4, 95.5), turned to 90 degrees
- moved C503 101.0 mm to (108.6, 113.4), turned to -135 degrees
- moved C505 98.1 mm to (109.5, 114.3), turned to -135 degrees
- moved R1801 97.9 mm to (120.4, 92.7)
- moved C507 95.3 mm to (110.4, 115.1), turned to -135 degrees
- moved JP1806 91.3 mm to (114.2, 98.8), turned to -90 degrees
- moved JP1807 91.3 mm to (114.2, 102.2), turned to -90 degrees
- moved JP1808 91.3 mm to (114.2, 105.5), turned to -90 degrees
- moved J1801 90.6 mm to (119.3, 100.4)
- moved JP1805 87.8 mm to (114.2, 95.4), turned to -90 degrees
- moved JP1801 82.4 mm to (118.6, 95.4), turned to -90 degrees
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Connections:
- net /SODIMM Connector/CANH_MCU renamed /SODIMM Connector/MCU_CAN+
- net /SODIMM Connector/CANL_MCU renamed /SODIMM Connector/MCU_CAN-
- C203 pad 1: /5V_RAW -> GND
- C203 pad 2: GNDPWR -> /5V_RAW
- C301 pad 2: GNDPWR -> GND
- C302 pad 2: GNDPWR -> GND
- C303 pad 2: GNDPWR -> GND
- C304 pad 2: GNDPWR -> GND
- C305 pad 2: GNDPWR -> GND
- C306 pad 2: GNDPWR -> GND
- D1402 pad 2: GNDPWR -> GND
- J1701 pad 2: /ST-link V2/USB Micro-B/USB_D- -> /ST-link V2/USB_D-
- J1701 pad 3: /ST-link V2/USB Micro-B/USB_D+ -> /ST-link V2/USB_D+
- J201 pad 1: /5V_RAW -> GND
- J201 pad 11: GNDPWR -> /5V_RAW
- J201 pad 13: GNDPWR -> /5V_RAW
- J201 pad 15: GNDPWR -> /5V_RAW
- J201 pad 17: GNDPWR -> /5V_RAW
- J201 pad 19: GNDPWR -> /5V_RAW
- J201 pad 3: /5V_RAW -> GND
- J201 pad 5: /5V_RAW -> GND
- J201 pad 7: /5V_RAW -> GND
- J201 pad 9: /5V_RAW -> GND
- JP1201 pad 2: /STM32L552ZET6Q/Peripherals/Debug LED Select/EN -> /Debug LED Array/EN
- JP1805 pad 2: +3.3V -> /ST-link V2/3V3_STLINK
- R1403 pad 1: GNDPWR -> GND
- R1407 pad 1: GNDPWR -> GND
- R1703 pad 1: /ST-link V2/USB Micro-B/USB_D- -> /ST-link V2/USB_D-
- R403 pad 2: /ST-link V2/3V3_STM -> +3.3V
- U1101 pad 6: /Debug LED Array/LED_ARR_EN -> /Debug LED Array/EN
- U1401 pad 4: GNDPWR -> GND
- U1401 pad 7: GNDPWR -> GND
- U1701 pad 1: /ST-link V2/USB Micro-B/USB_D+ -> /ST-link V2/USB_D+
- U1701 pad 2: /ST-link V2/USB Micro-B/USB_D- -> /ST-link V2/USB_D-
- U301 pad 3: GNDPWR -> GND
- U401 pad 32: /ST-link V2/USB.D- -> /ST-link V2/USB_D-
- U401 pad 33: /ST-link V2/USB.D+ -> /ST-link V2/USB_D+
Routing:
- net /5V_RAW: track 0.00 -> 52.9 mm, vias 0 -> 5
- net GND: track 0.00 -> 41.7 mm, vias 0 -> 29
- net +3.3V: track 0.00 -> 27.5 mm, vias 0 -> 27
- net /SODIMM Connector/MCU_CAN+: track 0.00 -> 26.7 mm, vias 0 -> 1
- net /SODIMM Connector/MCU_CAN-: track 0.00 -> 26.6 mm, vias 0 -> 1
- net /Power/Power Protection/3V3A_PROT: track 0.00 -> 22.6 mm
- net /ST-link V2/CAN_RX: track 0.00 -> 12.4 mm, vias 0 -> 1
- net Net-(U401-NRST): track 0.00 -> 9.03 mm, vias 0 -> 1
- net /ST-link V2/USB_D-: track 0.00 -> 7.89 mm
- net Net-(D1301-A): track 0.00 -> 7.86 mm, vias 0 -> 1
- net Net-(U401-PD1/OSCOUT): track 0.00 -> 7.00 mm
- net /ST-link V2/CAN_TX: track 0.00 -> 6.71 mm
- net /Power/Diagnostic LED/SIG: track 0.00 -> 6.57 mm, vias 0 -> 1
- net Net-(U401-PD0/OSCIN): track 0.00 -> 6.23 mm
- net Net-(JP504-A): track 0.00 -> 6.13 mm, vias 0 -> 1
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- added copper zone on B.Cu, net +3.3V
- added copper zone on F.Cu, net +3.3V
- added copper zone on In2.Cu, net +3.3V
- added copper zone on B.Cu, net /3V3A_RAW
- added copper zone on F.Cu, net /3V3A_RAW
- added copper zone on F.Cu, net /5V_RAW
- added copper zone on B.Cu, net /Power/Power Protection/5V_PROT
- added copper zone on F.Cu, net /Power/Power Protection/5V_PROT
